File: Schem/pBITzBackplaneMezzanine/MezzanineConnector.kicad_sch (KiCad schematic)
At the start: 17 parts, among them J5 FH69-60S-0.5SH, J6 pBITzBus, J7 FH69-60S-0.5SH, SW1 SW_Coded_SH-7030, SW2 SW_Coded_SH-7030, U5 74HC688, U6 74HC688

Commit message: Added all the manufacturer part numbers to the KiCad schematics and PCB files. This will make it easier to order the parts for the project and ensure that the correct components are used. I also removed some of the old schematics that were no longer needed, such as the BaudClock, ConsolePort, DeviceSelectDecode, GPIOUserSerial, IO Controller, UserPorts, Video, and Z80HomeBrew schematics. These changes will help to streamline the design and make it easier to understand.
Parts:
- J6: MANUFACTURER_PART_NUMBER (none) -> PCIE-098-02-F-D-RA
- R10, R7, R8, R9: MANUFACTURER_PART_NUMBER (none) -> RC0603FR-074K7L
- SW1, SW2: MANUFACTURER_PART_NUMBER (none) -> RDS-10S-7229-A-CR
- U5, U6: MANUFACTURER_PART_NUMBER (none) -> SN74HC688DWR
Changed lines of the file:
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@@
 			)
 		)
+		(property "MANUFACTURER_PART_NUMBER" "RC0603FR-074K7L"
+			(at 106.68 351.79 0)
+			(effects
+				(font
+					(size 1.27 1.27)
+				)
+				(hide yes)
+			)
+		)
 		(pin "1"
 		)
@@
 			)
 		)
+		(property "MANUFACTURER_PART_NUMBER" "RDS-10S-7229-A-CR"
+			(at 85.09 323.85 0)
+			(effects
+				(font
+					(size 1.27 1.27)
+				)
+				(hide yes)
+			)
+		)
 		(pin "1"
 		)
@@
 			)
 		)
+		(property "MANUFACTURER_PART_NUMBER" "PCIE-098-02-F-D-RA"
+			(at 457.2 154.94 0)
+			(effects
+				(font
+					(size 1.27 1.27)
+				)
+				(hide yes)
+			)
+		)
 		(pin "B26"
 		)
@@
 			)
 		)
+		(property "MANUFACTURER_PART_NUMBER" "SN74HC688DWR"
+			(at 186.69 341.63 0)
+			(effects
+				(font
+					(size 1.27 1.27)
+				)
+				(hide yes)
+			)
+		)
 		(pin "20"
 		)
@@
 			)
 		)
+		(property "MANUFACTURER_PART_NUMBER" "RC0603FR-074K7L"
+			(at 106.68 314.96 0)
+			(effects
+				(font
+					(size 1.27 1.27)
+				)
+				(hide yes)
+			)
+		)
 		(pin "1"
 		)
@@
 			)
 		)
+		(property "MANUFACTURER_PART_NUMBER" "RC0603FR-074K7L"
+			(at 114.3 351.79 0)
+			(effects
+				(font
+					(size 1.27 1.27)
+				)
+				(hide yes)
+			)
+		)
 		(pin "1"
 		)
@@
 			)
 		)
+		(property "MANUFACTURER_PART_NUMBER" "SN74HC688DWR"
+			(at 293.37 341.63 0)
+			(effects
+				(font
+					(size 1.27 1.27)
+				)
+				(hide yes)
+			)
+		)
 		(pin "20"
 		)
@@
 			)
 		)
+		(property "MANUFACTURER_PART_NUMBER" "PCIE-098-02-F-D-RA"
+			(at 373.38 111.76 0)
+			(effects
+				(font
+					(size 1.27 1.27)
+				)
+				(hide yes)
+			)
+		)
 		(pin "A26"
 		)
@@
 			)
 		)
+		(property "MANUFACTURER_PART_NUMBER" "RC0603FR-074K7L"
+			(at 114.3 314.96 0)
+			(effects
+				(font
+					(size 1.27 1.27)
+				)
+				(hide yes)
+			)
+		)
 		(pin "1"
 		)
@@
 			)
 		)
+		(property "MANUFACTURER_PART_NUMBER" "PCIE-098-02-F-D-RA"
+			(at 457.2 189.23 0)
+			(effects
+				(font
+					(size 1.27 1.27)
+				)
+				(hide yes)
+			)
+		)
 		(pin "B26"
 		)
@@
 			(at 85.09 360.68 0)
 			(effects
+				(font
+					(size 1.27 1.27)
+				)
+				(hide yes)
+			)
+		)
+		(property "MANUFACTURER_PART_NUMBER" "RDS-10S-7229-A-CR"
+			(at 85.09 360.68 0)
+			(effects

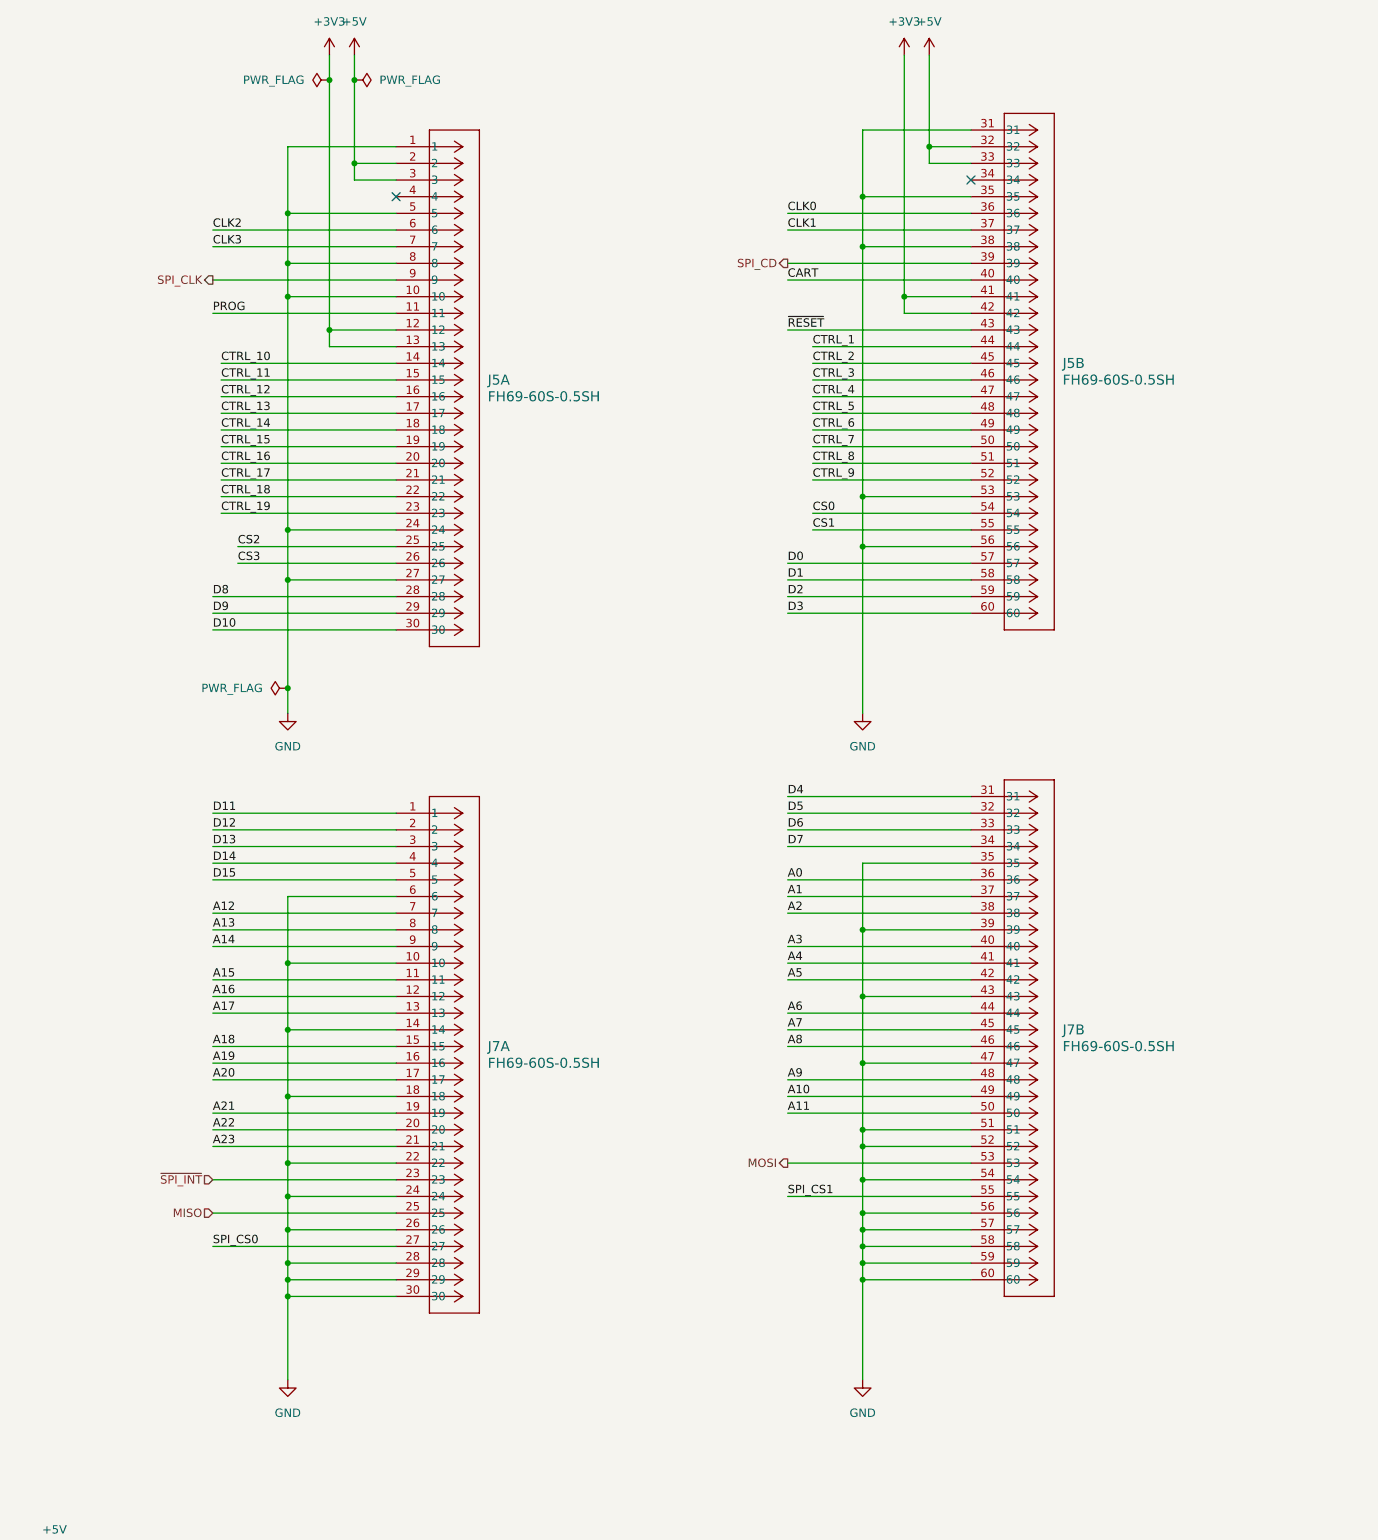
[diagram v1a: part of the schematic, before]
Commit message: * Corrected the reversal of the flat connector cable  * Added copper pours
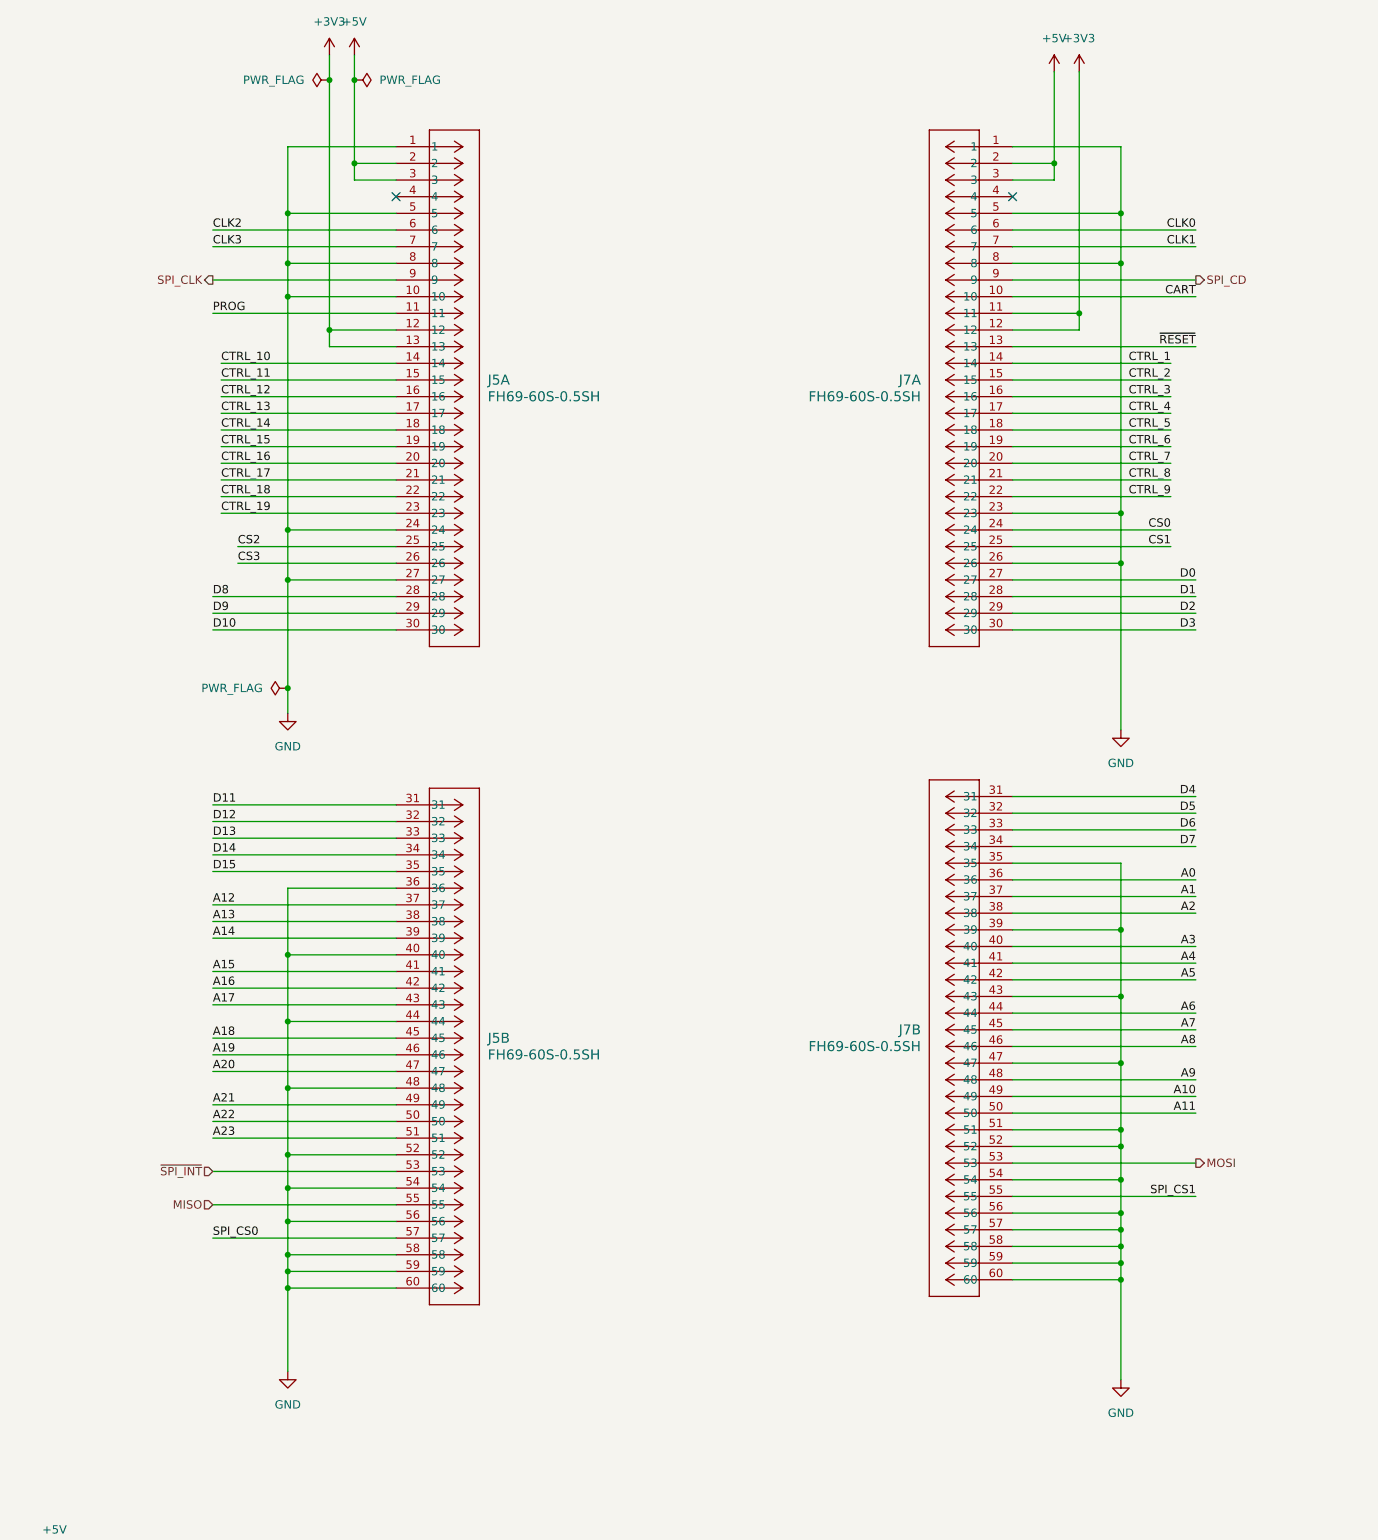
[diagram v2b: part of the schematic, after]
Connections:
- net +3V3: now also J7.11, J7.12; no longer J5.41, J5.42
- net +5V: now also J7.2, J7.3; no longer J5.32, J5.33
- net A12: now also J5.37; no longer J7.7
- net A13: now also J5.38; no longer J7.8
- net A14: now also J5.39; no longer J7.9
- net A15: now also J5.41; no longer J7.11
- net A16: now also J5.42; no longer J7.12
- net A17: now also J5.43; no longer J7.13
- net A18: now also J5.45; no longer J7.15
- net A19: now also J5.46; no longer J7.16
- net A20: now also J5.47; no longer J7.17
- net A21: now also J5.49; no longer J7.19
- net A22: now also J5.50; no longer J7.20
- net A23: now also J5.51; no longer J7.21
- net CART: now also J7.10; no longer J5.40
- net CLK0: now also J7.6; no longer J5.36
- net CLK1: now also J7.7; no longer J5.37
- net CS0: now also J7.24; no longer J5.54
- net CS1: now also J7.25; no longer J5.55
- net CTRL_1: now also J7.14; no longer J5.44
- net CTRL_2: now also J7.15; no longer J5.45
- net CTRL_3: now also J7.16; no longer J5.46
- net CTRL_4: now also J7.17; no longer J5.47
- net CTRL_5: now also J7.18; no longer J5.48
- net CTRL_6: now also J7.19; no longer J5.49
- net CTRL_7: now also J7.20; no longer J5.50
- net CTRL_8: now also J7.21; no longer J5.51
- net CTRL_9: now also J7.22; no longer J5.52
- net D0: now also J7.27; no longer J5.57
- net D1: now also J7.28; no longer J5.58
- net D11: now also J5.31; no longer J7.1
- net D12: now also J5.32; no longer J7.2
- net D13: now also J5.33; no longer J7.3
- net D14: now also J5.34; no longer J7.4
- net D15: now also J5.35; no longer J7.5
- net D2: now also J7.29; no longer J5.59
- net D3: now also J7.30; no longer J5.60
- net GND: now also J5.36, J5.40, J5.44, J5.48, J5.52, J5.54, J5.58, J5.59, J5.60, J7.1, J7.23, J7.5, J7.8; no longer J5.31, J5.35, J5.38, J5.53, J7.10, J7.14, J7.18, J7.22, J7.24, J7.28, J7.29, J7.30, J7.6
- net MISO: now also J5.55; no longer J7.25
- net SPI_CD: now also J7.9; no longer J5.39
- net SPI_CS0: now also J5.57; no longer J7.27
- net ~{RESET}: now also J7.13; no longer J5.43
- net ~{SPI_INT}: now also J5.53; no longer J7.23
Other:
- moved on the sheet: J5B, J7A, J7B

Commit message: Small errors in BOM
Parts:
- C16, C17: footprint Capacitor_SMD:C_0504_1310Metric_Pad0.83x1.28mm_HandSolder -> Capacitor_SMD:C_0603_1608Metric; MANUFACTURER_PART_NUMBER (none) -> C0603C104K5RACTU
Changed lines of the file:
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@@
 			)
 		)
-		(property "Footprint" "Capacitor_SMD:C_0504_1310Metric_Pad0.83x1.28mm_HandSolder"
+		(property "Footprint" "Capacitor_SMD:C_0603_1608Metric"
 			(at 360.3752 316.23 0)
 			(effects
@@
 		)
 		(property "Description" "Unpolarized capacitor"
+			(at 359.41 312.42 0)
+			(effects
+				(font
+					(size 1.27 1.27)
+				)
+				(hide yes)
+			)
+		)
+		(property "MANUFACTURER_PART_NUMBER" "C0603C104K5RACTU"
 			(at 359.41 312.42 0)
 			(effects
@@
 			)
 		)
-		(property "Footprint" "Capacitor_SMD:C_0504_1310Metric_Pad0.83x1.28mm_HandSolder"
+		(property "Footprint" "Capacitor_SMD:C_0603_1608Metric"
 			(at 373.0752 316.23 0)
 			(effects
@@
 			(at 372.11 312.42 0)
 			(effects
+				(font
+					(size 1.27 1.27)
+				)
+				(hide yes)
+			)
+		)
+		(property "MANUFACTURER_PART_NUMBER" "C0603C104K5RACTU"
+			(at 372.11 312.42 0)
+			(effects

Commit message: Major rework:
- Updated the Mezzanine to remove the slot connector and move it to the main board (facing the back)
-    The removal of the slot allowed for the removal of the FPC connector, which was a
     major source of complexity. The mezzanine now only has the SD card and USB connectors,
     which are much cheaper and easier to work with.
- The mezzanine is now more compact and cheaper to souirce

- The main board sees the addition of the external slot connector (coming from the mezzanine)
- Added power led on the mother board for easier debugging and testing
- Removed the free floating resistors to replace them with resistor packs
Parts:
- removed J5, J7: FH69-60S-0.5SH, Footprints:CONN60_FH69-60S_HIR, symbol 2026-01-31_22-05-17:FH69-60S-0.5SH
- removed J6: pBITzBus, Footprints:SAMTEC_PCIE-098-02-X-D-RA, symbol pBITz:pBITzBus
- added J5: Conn_02x10_Odd_Even, Connector_IDC:IDC-Header_2x10_P2.54mm_Vertical, symbol Connector_Generic:Conn_02x10_Odd_Even
- H1, H2, H3, H4: footprint MountingHole:MountingHole_3.2mm_M3 -> MountingHole:MountingHole_3.2mm_M3_Pad
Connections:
- net +3V3: now also J5.2 (Pin_2)
- net +5V: now also J5.1 (Pin_1)
- net GND: now also J5.10 (Pin_10), J5.11 (Pin_11), J5.14 (Pin_14), J5.15 (Pin_15), J5.16 (Pin_16), J5.18 (Pin_18), J5.19 (Pin_19), J5.20 (Pin_20), J5.6 (Pin_6), J5.7 (Pin_7)
- net MISO: now also J5.5 (Pin_5)
- net MOSI: now also J5.3 (Pin_3)
- net SPI_CLK: now also J5.9 (Pin_9)
- net SPI_CS0: now also J5.4 (Pin_4)
- net SPI_CS1: now also J5.8 (Pin_8)
- net ~{SPI_INT}: now also J5.13 (Pin_13)
- new net ~{SD_PRESENT}: J5.17 (Pin_17)
- no-connect marks 15 -> 5

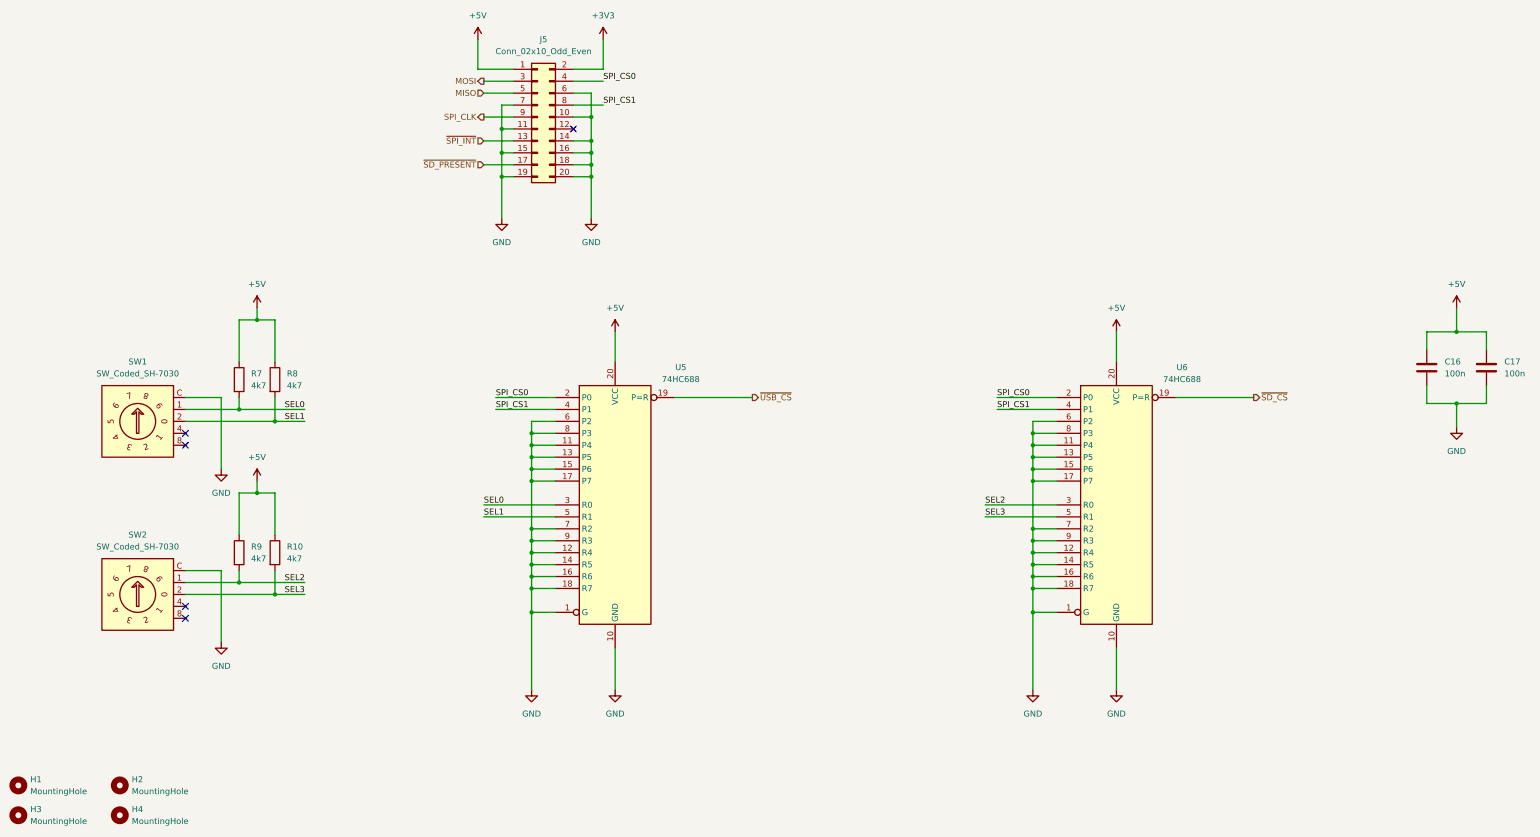
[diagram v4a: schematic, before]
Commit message: Removed the rotary switch selector
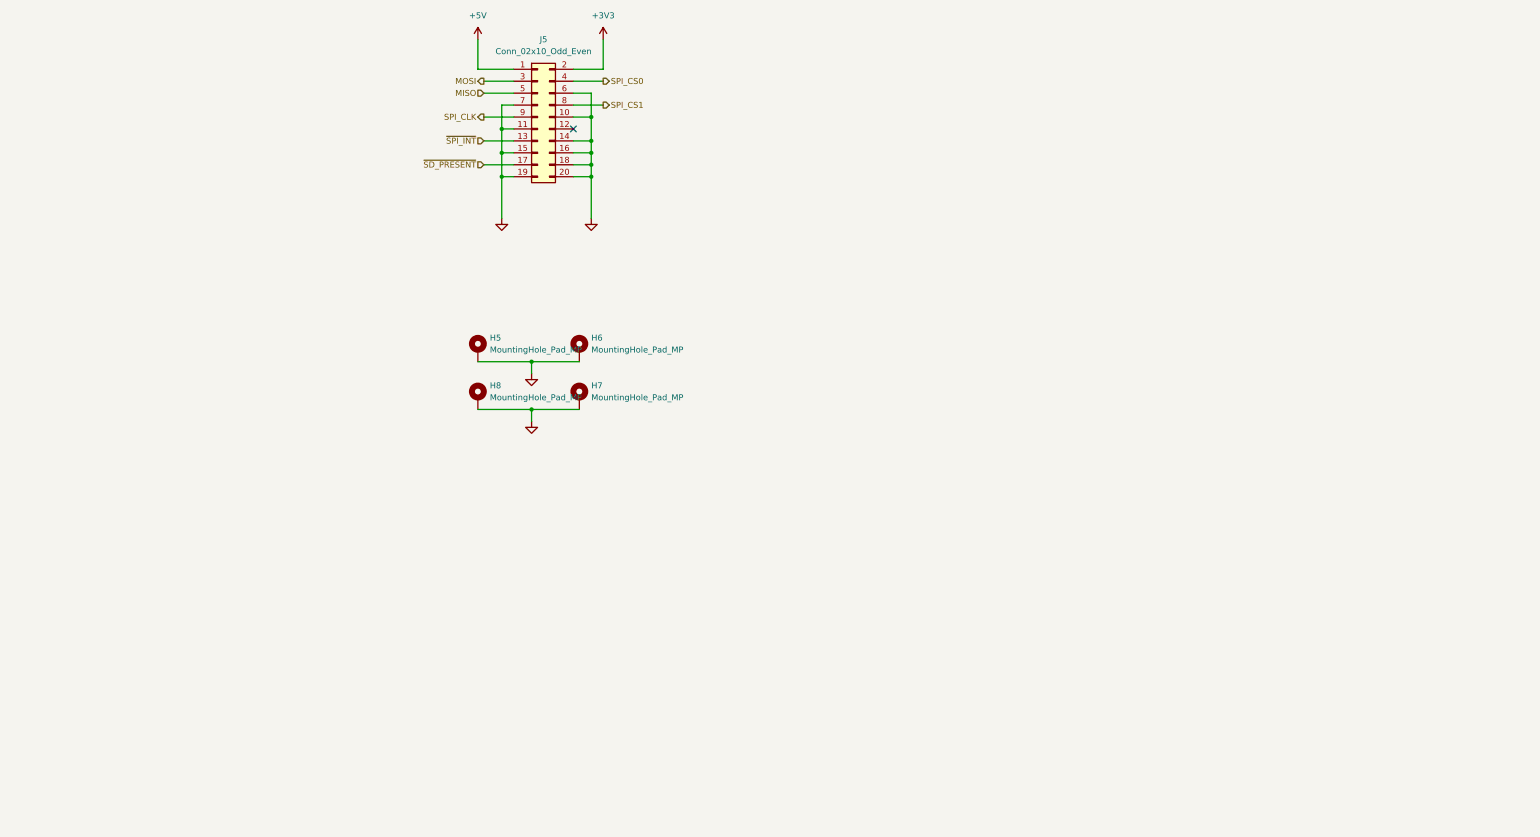
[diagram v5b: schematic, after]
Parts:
- removed C16, C17: 100n, Capacitor_SMD:C_0603_1608Metric, symbol Device:C
- removed H1, H2, H3, H4: MountingHole, MountingHole:MountingHole_3.2mm_M3_Pad, symbol Mechanical:MountingHole
- removed R10, R7, R8, R9: 4k7, Resistor_SMD:R_0603_1608Metric, symbol Device:R
- removed SW1, SW2: SW_Coded_SH-7030, Button_Switch_THT:Nidec_Copal_SH-7010C, symbol Switch:SW_Coded_SH-7030
- removed U5, U6: 74HC688, Package_SO:SOIC-20W_7.5x12.8mm_P1.27mm, symbol 74xx:74HC688
- added H5, H6, H7, H8: MountingHole_Pad_MP, MountingHole:MountingHole_3.2mm_M3_Pad_TopBottom, symbol Mechanical:MountingHole_Pad_MP
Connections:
- net GND: now also H5.MP, H6.MP, H7.MP, H8.MP
- no-connect marks 5 -> 1
